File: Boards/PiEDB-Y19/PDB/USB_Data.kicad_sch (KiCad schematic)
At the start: 9 parts, among them J3 USB_B, U2 CH340G, Y1 12MHz

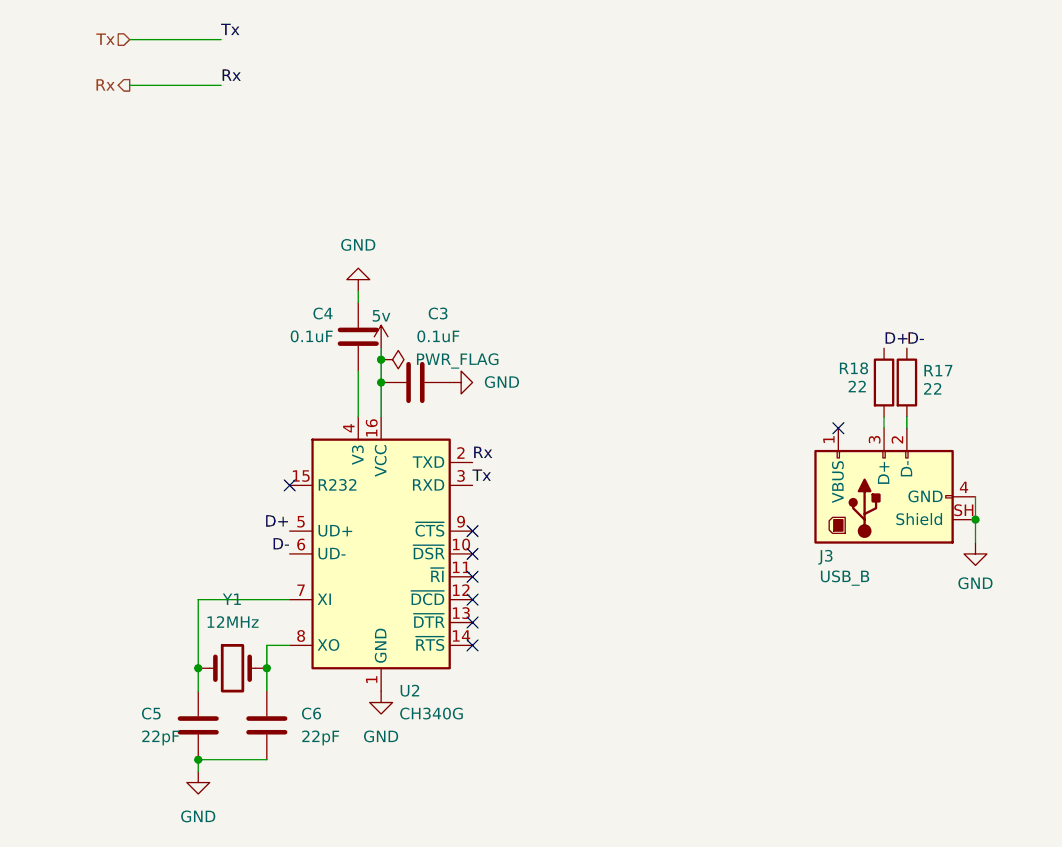
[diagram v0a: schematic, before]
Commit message: replaced pro micro and CH340G with ATMEGA32U4, added LM66100 power ORing, status LEDs, digit PNP drivers, and USB ESD; INITIAL LAYOUT
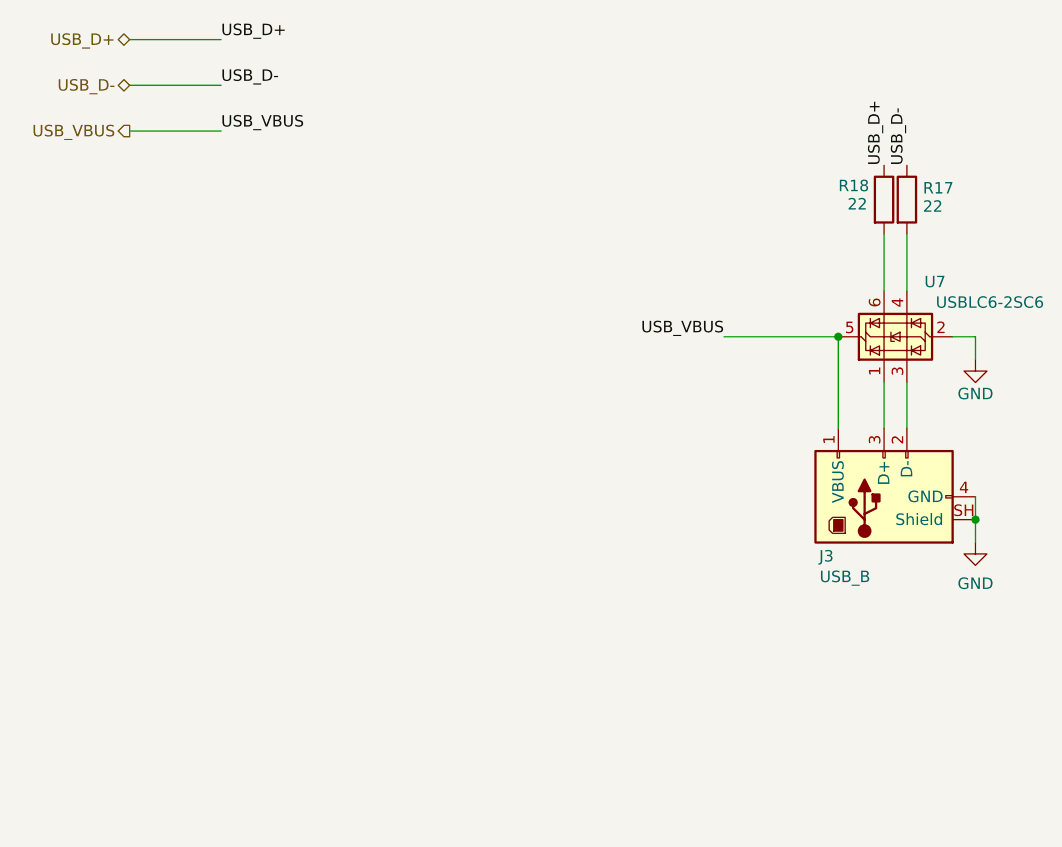
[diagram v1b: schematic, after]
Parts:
- removed C3, C4: 0.1uF, Capacitor_SMD:C_0603_1608Metric, symbol Device:C
- removed C5, C6: 22pF, Capacitor_SMD:C_0603_1608Metric, symbol Device:C
- removed U2: CH340G, PiE_Footprints:CH340g, symbol Interface_USB:CH340G
- removed Y1: 12MHz, PiE_Footprints:JYJE S1C12000VWFAC, symbol Device:Crystal
- added U7: USBLC6-2SC6, Package_TO_SOT_SMD:SOT-23-6, symbol Power_Protection:USBLC6-2SC6
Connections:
- net GND: now also U7.2 (GND)
- net at R17.2: now also U7.4 (I/O2); no longer J3.2 (D-)
- net at R18.2: now also U7.6 (I/O1); no longer J3.3 (D+)
- net USB_VBUS: now reaches J3.1 (VBUS)
- net USB_VBUS: now also U7.5 (VBUS)
- net D+ renamed USB_D+
- net D- renamed USB_D-
- new net: J3.2 (D-), U7.3 (I/O2)
- new net: J3.3 (D+), U7.1 (I/O1)
- no-connect marks 8 -> 0
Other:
- moved on the sheet: R17, R18

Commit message: rerouted PDB to final satisfaction; need to add testpoints
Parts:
- J3: footprint Connector_USB:USB_B_OST_USB-B1HSxx_Horizontal -> PiE_Footprints:USB_B_OST_USB-B1HSxx_Horizontal
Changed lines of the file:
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@@
 			)
 		)
-		(property "Footprint" "Connector_USB:USB_B_OST_USB-B1HSxx_Horizontal"
+		(property "Footprint" "PiE_Footprints:USB_B_OST_USB-B1HSxx_Horizontal"
 			(at 110.49 72.39 0)
 			(hide yes)
